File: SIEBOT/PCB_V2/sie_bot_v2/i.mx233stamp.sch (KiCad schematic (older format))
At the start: 0 parts

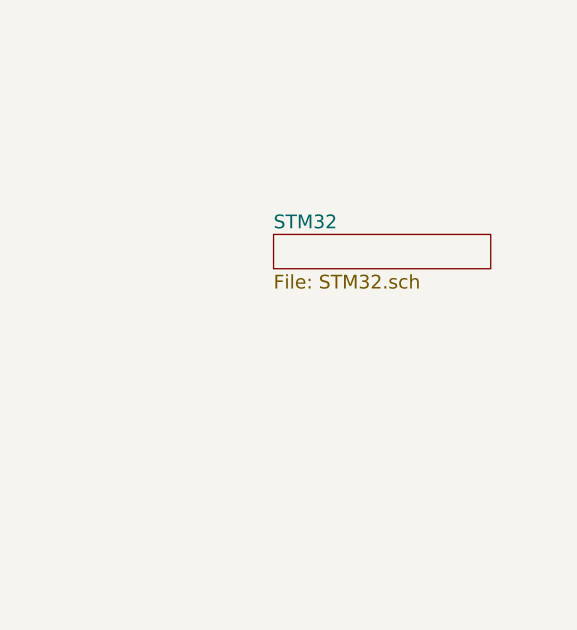
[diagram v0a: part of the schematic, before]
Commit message: Adición de programadores con ejemplos de manejo de los diferentes periféricos
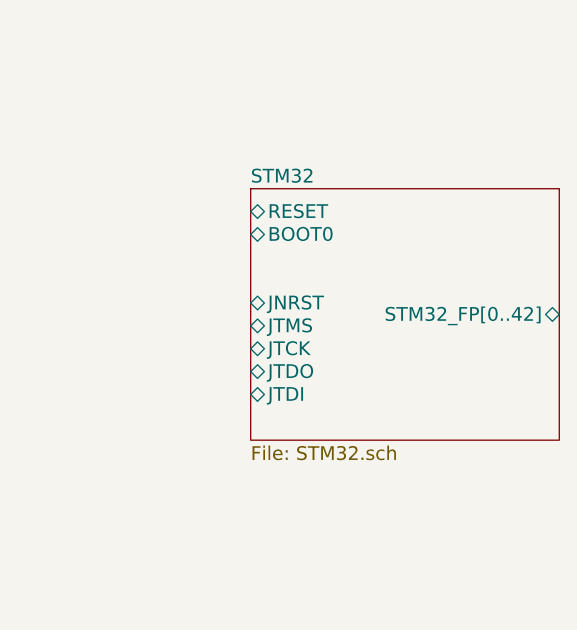
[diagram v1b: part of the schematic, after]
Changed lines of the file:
@@
-EESchema Schematic File Version 2  date Tue 20 Sep 2011 03:35:58 PM COT
+EESchema Schematic File Version 2  date Wed 21 Sep 2011 02:34:46 PM COT
 LIBS:con-jack
 LIBS:adm3101e
@@
 Sheet 1 5
 Title ""
-Date "20 sep 2011"
+Date "21 sep 2011"
 Rev ""
 Comp ""
@@
 $EndDescr
 $Sheet
-S 7700 2450 950  150
+S 7600 2250 1350 1100
 U 4E78AF25
 F0 "STM32" 60
 F1 "STM32.sch" 60
+F2 "BOOT0" B L 7600 2450 60
+F3 "JNRST" B L 7600 2750 60
+F4 "JTMS" B L 7600 2850 60
+F5 "JTCK" B L 7600 2950 60
+F6 "JTDO" B L 7600 3050 60
+F7 "JTDI" B L 7600 3150 60
+F8 "RESET" B L 7600 2350 60
+F9 "STM32_FP[0..42]" B R 8950 2800 60
 $EndSheet
 Wire Wire Line

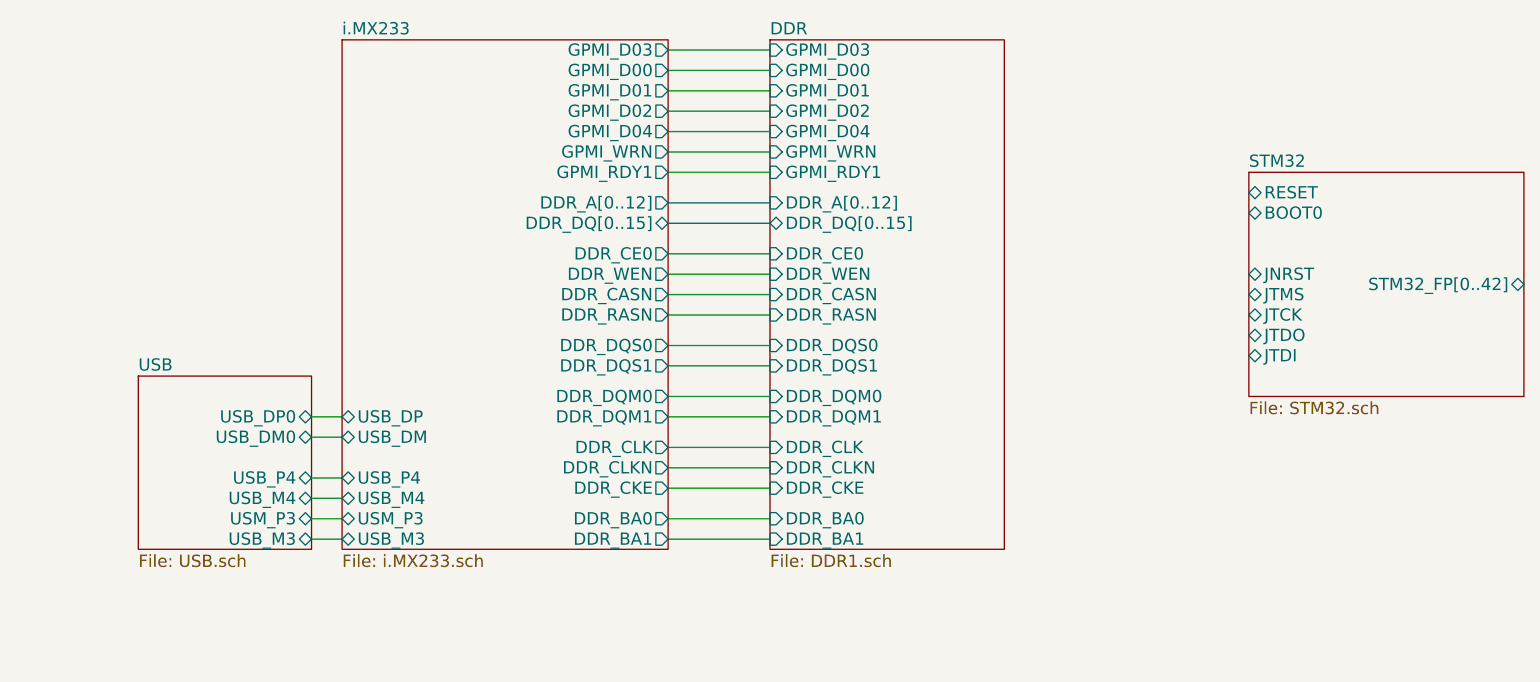
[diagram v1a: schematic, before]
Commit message: Conexión del STM32 con el procesador, adición de un regulador de 3.3V disponible para el usuario
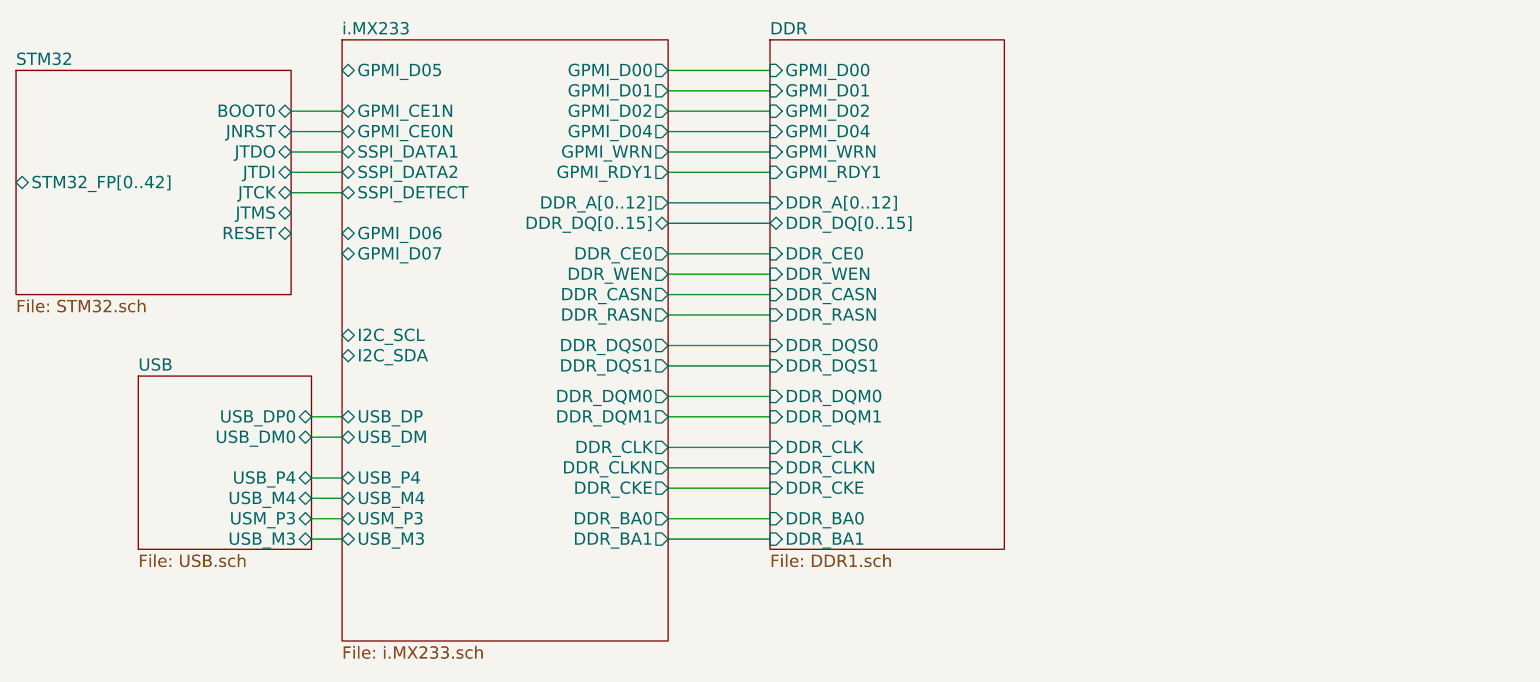
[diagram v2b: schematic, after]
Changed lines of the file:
@@
-EESchema Schematic File Version 2  date Wed 21 Sep 2011 02:34:46 PM COT
+EESchema Schematic File Version 2  date Wed 28 Sep 2011 07:26:12 AM COT
 LIBS:con-jack
 LIBS:adm3101e
@@
 LIBS:Reset
 LIBS:stm32f100vxx
+LIBS:lt1117cst
 LIBS:i.mx233stamp-cache
 EELAYER 25  0
@@
 Sheet 1 5
 Title ""
-Date "21 sep 2011"
+Date "28 sep 2011"
 Rev ""
 Comp ""
@@
 Comment4 ""
 $EndDescr
-$Sheet
-S 7600 2250 1350 1100
-U 4E78AF25
-F0 "STM32" 60
-F1 "STM32.sch" 60
-F2 "BOOT0" B L 7600 2450 60
-F3 "JNRST" B L 7600 2750 60
-F4 "JTMS" B L 7600 2850 60
-F5 "JTCK" B L 7600 2950 60
-F6 "JTDO" B L 7600 3050 60
-F7 "JTDI" B L 7600 3150 60
-F8 "RESET" B L 7600 2350 60
-F9 "STM32_FP[0..42]" B R 8950 2800 60
-$EndSheet
+Wire Wire Line
+	2900 2250 3150 2250
+Wire Wire Line
+	2900 2050 3150 2050
 Wire Wire Line
 	3000 4050 3150 4050
@@
 Wire Wire Line
 	3000 3550 3150 3550
-Wire Wire Line
-	4750 1650 5250 1650
 Wire Wire Line
 	4750 2250 5250 2250
@@
 Wire Wire Line
 	3000 3950 3150 3950
-$Sheet
-S 2150 3250 850  850
-U 4E3BEC51
-F0 "USB" 60
-F1 "USB.sch" 60
-F2 "USB_DM0" T R 3000 3550 60
-F3 "USB_DP0" T R 3000 3450 60
-F4 "USB_P4" B R 3000 3750 60
-F5 "USB_M4" B R 3000 3850 60
-F6 "USM_P3" B R 3000 3950 60
-F7 "USB_M3" B R 3000 4050 60
+Wire Wire Line
+	2900 1950 3150 1950
+Wire Wire Line
+	2900 2150 3150 2150
+Wire Wire Line
+	2900 2350 3150 2350
+$Sheet
+S 3150 1600 1600 2950
+U 4D30AC69
+F0 "i.MX233" 60
+F1 "i.MX233.sch" 60
+F2 "DDR_A[0..12]" O R 4750 2400 60
+F3 "DDR_DQ[0..15]" B R 4750 2500 60
+F4 "DDR_WEN" O R 4750 2750 60
+F5 "DDR_RASN" O R 4750 2950 60
+F6 "DDR_DQS1" O R 4750 3200 60
+F7 "DDR_DQS0" O R 4750 3100 60
+F8 "DDR_DQM1" O R 4750 3450 60
+F9 "DDR_DQM0" O R 4750 3350 60
+F10 "DDR_CLK" O R 4750 3600 60
+F11 "DDR_CLKN" O R 4750 3700 60
+F12 "DDR_CKE" O R 4750 3800 60
+F13 "DDR_CASN" O R 4750 2850 60
+F14 "DDR_CE0" O R 4750 2650 60
+F15 "DDR_BA1" O R 4750 4050 60
+F16 "DDR_BA0" O R 4750 3950 60
+F17 "GPMI_D04" O R 4750 2050 60
+F18 "GPMI_WRN" O R 4750 2150 60
+F19 "GPMI_RDY1" O R 4750 2250 60
+F20 "GPMI_D00" O R 4750 1750 60
+F21 "GPMI_D01" O R 4750 1850 60
+F22 "GPMI_D02" O R 4750 1950 60
+F23 "USB_DM" B L 3150 3550 60
+F24 "USB_DP" B L 3150 3450 60
+F25 "USB_M3" B L 3150 4050 60
+F26 "USM_P3" B L 3150 3950 60
+F27 "USB_M4" B L 3150 3850 60
+F28 "USB_P4" B L 3150 3750 60
+F29 "I2C_SCL" B L 3150 3050 60
+F30 "I2C_SDA" B L 3150 3150 60
+F31 "GPMI_CE0N" B L 3150 2050 60
+F32 "SSPI_DATA1" B L 3150 2150 60
+F33 "SSPI_DETECT" B L 3150 2350 60
+F34 "SSPI_DATA2" B L 3150 2250 60
+F35 "GPMI_D05" B L 3150 1750 60
+F36 "GPMI_CE1N" B L 3150 1950 60
+F37 "GPMI_D06" B L 3150 2550 60
+F38 "GPMI_D07" B L 3150 2650 60
 $EndSheet
 $Sheet
@@
 F21 "GPMI_D01" I L 5250 1850 60
 F22 "GPMI_D00" I L 5250 1750 60
-F23 "GPMI_D03" I L 5250 1650 60
-$EndSheet
-$Sheet
-S 3150 1600 1600 2500
-U 4D30AC69
-F0 "i.MX233" 60
-F1 "i.MX233.sch" 60
-F2 "DDR_A[0..12]" O R 4750 2400 60
-F3 "DDR_DQ[0..15]" B R 4750 2500 60
-F4 "DDR_WEN" O R 4750 2750 60
-F5 "DDR_RASN" O R 4750 2950 60
-F6 "DDR_DQS1" O R 4750 3200 60
-F7 "DDR_DQS0" O R 4750 3100 60
-F8 "DDR_DQM1" O R 4750 3450 60
-F9 "DDR_DQM0" O R 4750 3350 60
-F10 "DDR_CLK" O R 4750 3600 60
-F11 "DDR_CLKN" O R 4750 3700 60
-F12 "DDR_CKE" O R 4750 3800 60
-F13 "DDR_CASN" O R 4750 2850 60
-F14 "DDR_CE0" O R 4750 2650 60
-F15 "DDR_BA1" O R 4750 4050 60
-F16 "DDR_BA0" O R 4750 3950 60
-F17 "GPMI_D04" O R 4750 2050 60
-F18 "GPMI_WRN" O R 4750 2150 60
-F19 "GPMI_RDY1" O R 4750 2250 60
-F20 "GPMI_D00" O R 4750 1750 60
-F21 "GPMI_D01" O R 4750 1850 60
-F22 "GPMI_D02" O R 4750 1950 60
-F23 "GPMI_D03" O R 4750 1650 60
-F24 "USB_DM" B L 3150 3550 60
-F25 "USB_DP" B L 3150 3450 60
-F26 "USB_M3" B L 3150 4050 60
-F27 "USM_P3" B L 3150 3950 60
-F28 "USB_M4" B L 3150 3850 60
-F29 "USB_P4" B L 3150 3750 60
+$EndSheet
+$Sheet
+S 1550 1750 1350 1100
+U 4E78AF25
+F0 "STM32" 60
+F1 "STM32.sch" 60
+F2 "BOOT0" B R 2900 1950 60
+F3 "JNRST" B R 2900 2050 60
+F4 "JTMS" B R 2900 2450 60
+F5 "JTCK" B R 2900 2350 60
+F6 "JTDO" B R 2900 2150 60
+F7 "JTDI" B R 2900 2250 60
+F8 "RESET" B R 2900 2550 60
+F9 "STM32_FP[0..42]" B L 1550 2300 60
+$EndSheet
+$Sheet
+S 2150 3250 850  850
+U 4E3BEC51
+F0 "USB" 60
+F1 "USB.sch" 60
+F2 "USB_DM0" T R 3000 3550 60
+F3 "USB_DP0" T R 3000 3450 60
+F4 "USB_P4" B R 3000 3750 60
+F5 "USB_M4" B R 3000 3850 60
+F6 "USM_P3" B R 3000 3950 60
+F7 "USB_M3" B R 3000 4050 60
 $EndSheet
 $EndSCHEMATC

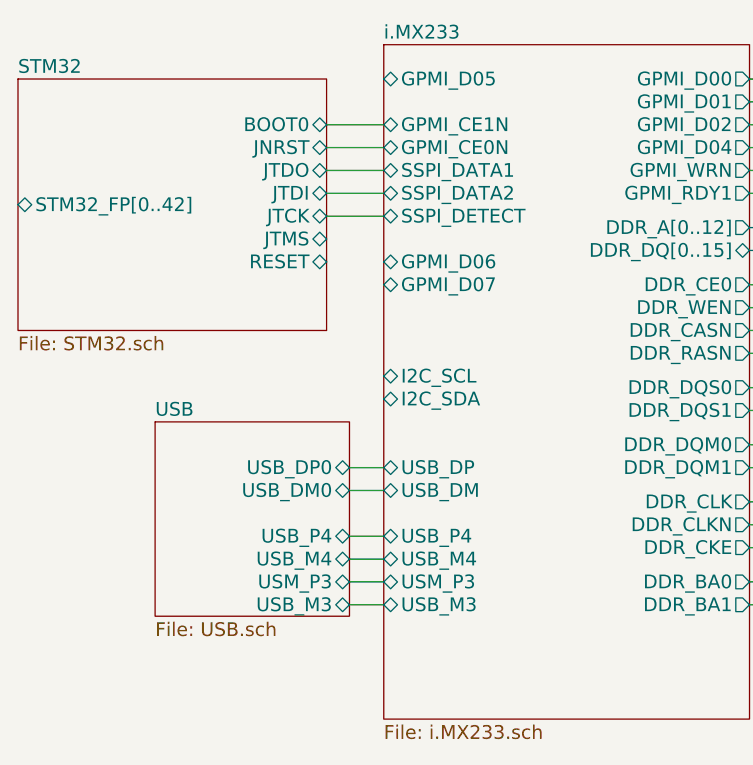
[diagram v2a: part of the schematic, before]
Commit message: Ruteo de la conexión entre el procesador y el STM32, re-localización de los conectores de alimentación y USB, adidición del regulador de 3.3V
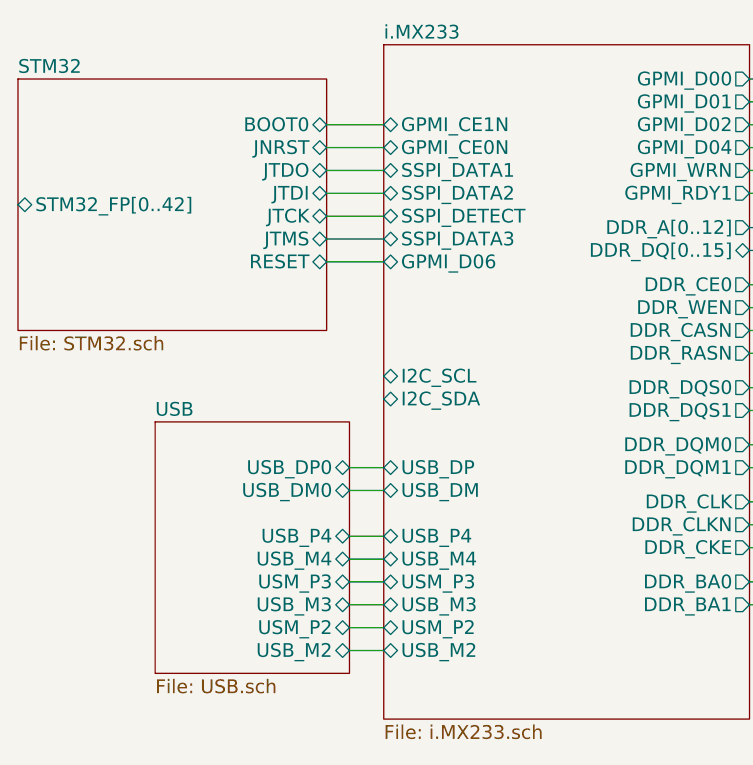
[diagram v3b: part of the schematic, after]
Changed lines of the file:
@@
-EESchema Schematic File Version 2  date Wed 28 Sep 2011 07:26:12 AM COT
+EESchema Schematic File Version 2  date Wed 28 Sep 2011 02:09:01 PM COT
 LIBS:con-jack
 LIBS:adm3101e
@@
 $EndDescr
 Wire Wire Line
+	3000 4250 3150 4250
+Wire Wire Line
+	2900 2550 3150 2550
+Wire Wire Line
 	2900 2250 3150 2250
 Wire Wire Line
@@
 Wire Wire Line
 	2900 2350 3150 2350
+Wire Wire Line
+	2900 2450 3150 2450
+Wire Wire Line
+	3000 4150 3150 4150
 $Sheet
 S 3150 1600 1600 2950
@@
 F33 "SSPI_DETECT" B L 3150 2350 60
 F34 "SSPI_DATA2" B L 3150 2250 60
-F35 "GPMI_D05" B L 3150 1750 60
-F36 "GPMI_CE1N" B L 3150 1950 60
-F37 "GPMI_D06" B L 3150 2550 60
-F38 "GPMI_D07" B L 3150 2650 60
+F35 "GPMI_CE1N" B L 3150 1950 60
+F36 "GPMI_D06" B L 3150 2550 60
+F37 "SSPI_DATA3" B L 3150 2450 60
+F38 "USM_P2" B L 3150 4150 60
+F39 "USB_M2" B L 3150 4250 60
 $EndSheet
 $Sheet
@@
 $EndSheet
 $Sheet
-S 2150 3250 850  850
+S 2150 3250 850  1100
 U 4E3BEC51
 F0 "USB" 60
@@
 F6 "USM_P3" B R 3000 3950 60
 F7 "USB_M3" B R 3000 4050 60
+F8 "USB_M2" B R 3000 4250 60
+F9 "USM_P2" B R 3000 4150 60
 $EndSheet
 $EndSCHEMATC

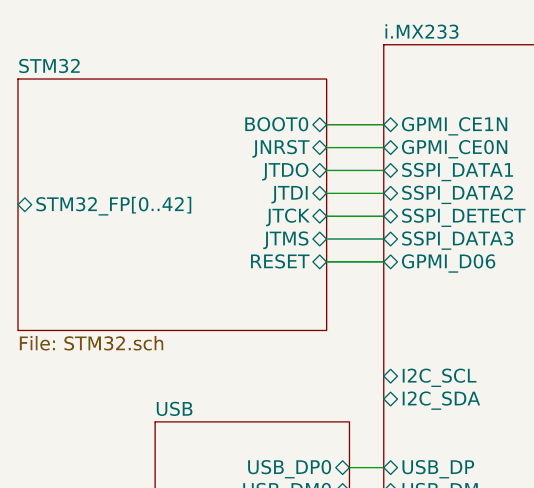
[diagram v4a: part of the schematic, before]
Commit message: Adición de puentes H, finalización del ruteo de los pines del STM32
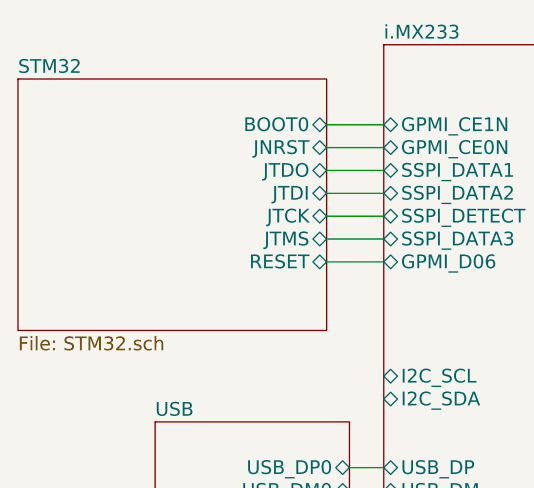
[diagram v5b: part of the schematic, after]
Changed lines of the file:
@@
-EESchema Schematic File Version 2  date Fri 30 Sep 2011 11:20:00 AM COT
+EESchema Schematic File Version 2  date Fri 30 Sep 2011 12:13:05 PM COT
 LIBS:con-jack
 LIBS:adm3101e
@@
 LIBS:stm32f100vxx
 LIBS:lt1117cst
+LIBS:zxmhc3f381n8
 LIBS:i.mx233stamp-cache
 EELAYER 25  0
@@
 Comment4 ""
 $EndDescr
+$Sheet
+S 1550 1750 1350 1100
+U 4E78AF25
+F0 "STM32" 60
+F1 "STM32.sch" 60
+F2 "BOOT0" B R 2900 1950 60
+F3 "JNRST" B R 2900 2050 60
+F4 "JTMS" B R 2900 2450 60
+F5 "JTCK" B R 2900 2350 60
+F6 "JTDO" B R 2900 2150 60
+F7 "JTDI" B R 2900 2250 60
+F8 "RESET" B R 2900 2550 60
+$EndSheet
 Wire Wire Line
 	3000 4250 3150 4250
@@
 $EndSheet
 $Sheet
-S 1550 1750 1350 1100
-U 4E78AF25
-F0 "STM32" 60
-F1 "STM32.sch" 60
-F2 "BOOT0" B R 2900 1950 60
-F3 "JNRST" B R 2900 2050 60
-F4 "JTMS" B R 2900 2450 60
-F5 "JTCK" B R 2900 2350 60
-F6 "JTDO" B R 2900 2150 60
-F7 "JTDI" B R 2900 2250 60
-F8 "RESET" B R 2900 2550 60
-F9 "STM32_FP[0..42]" B L 1550 2300 60
-$EndSheet
-$Sheet
